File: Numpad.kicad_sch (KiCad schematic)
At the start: 107 parts, among them J1 USB_C_Receptacle_USB2.0, J3 AVR-ISP-6, Q2 DMN2041L, SW10 SW_Push, SW11 SW_Push, SW12 SW_Push, SW13 SW_Push, SW14 SW_Push, SW15 SW_Push, SW16 SW_Push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

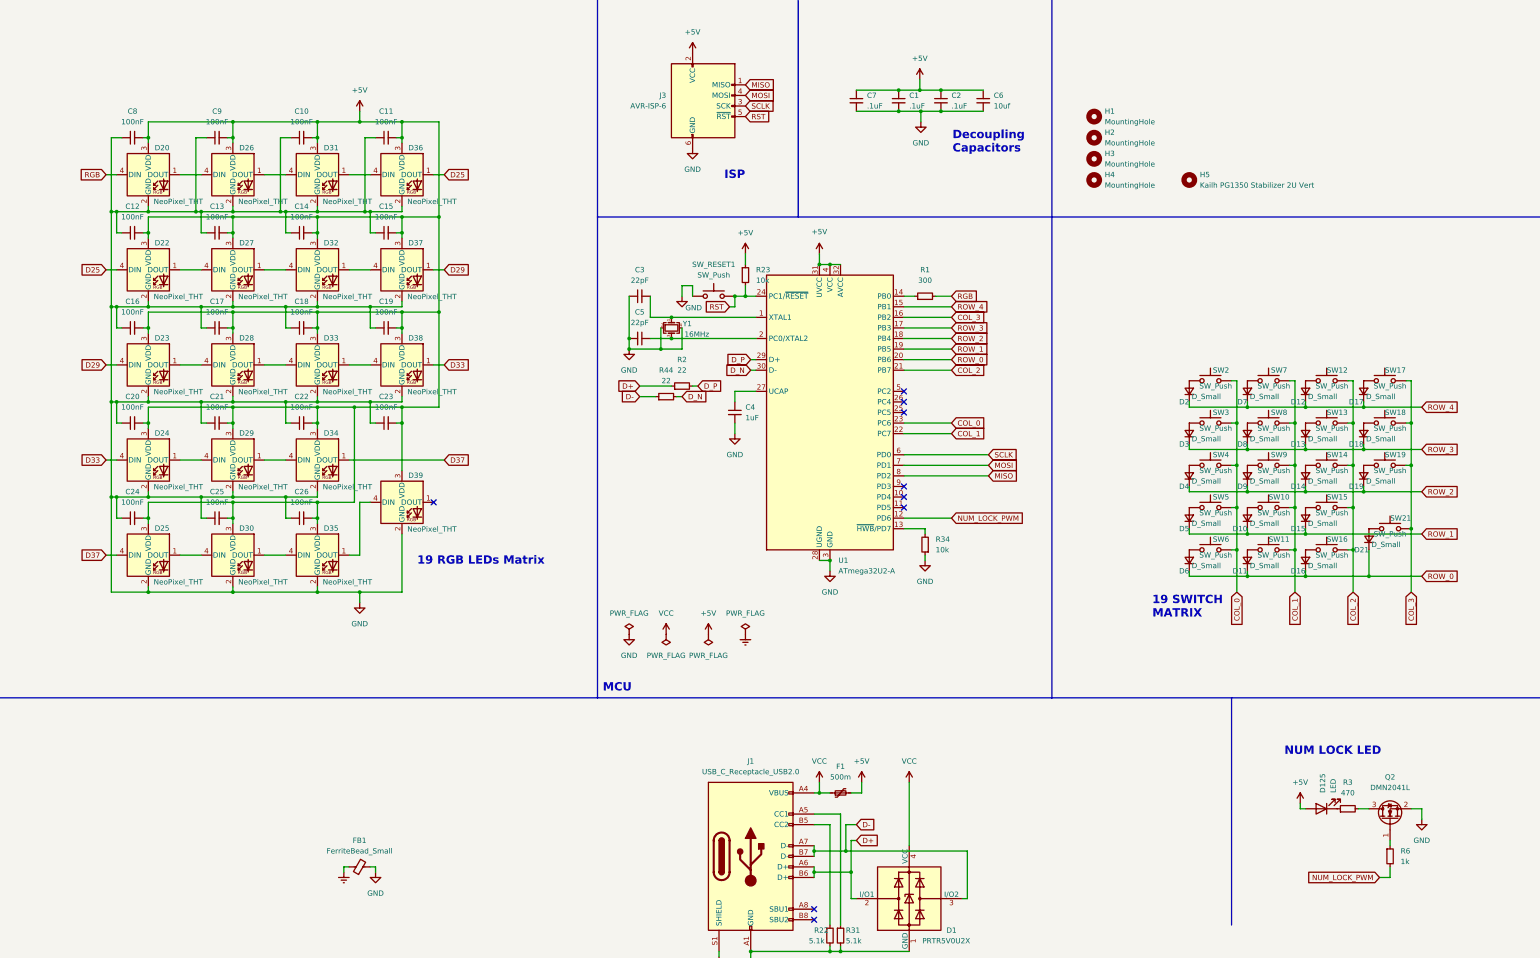
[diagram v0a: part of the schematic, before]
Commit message: replaced LEDs with RGBs, and started the PCB for keyboard
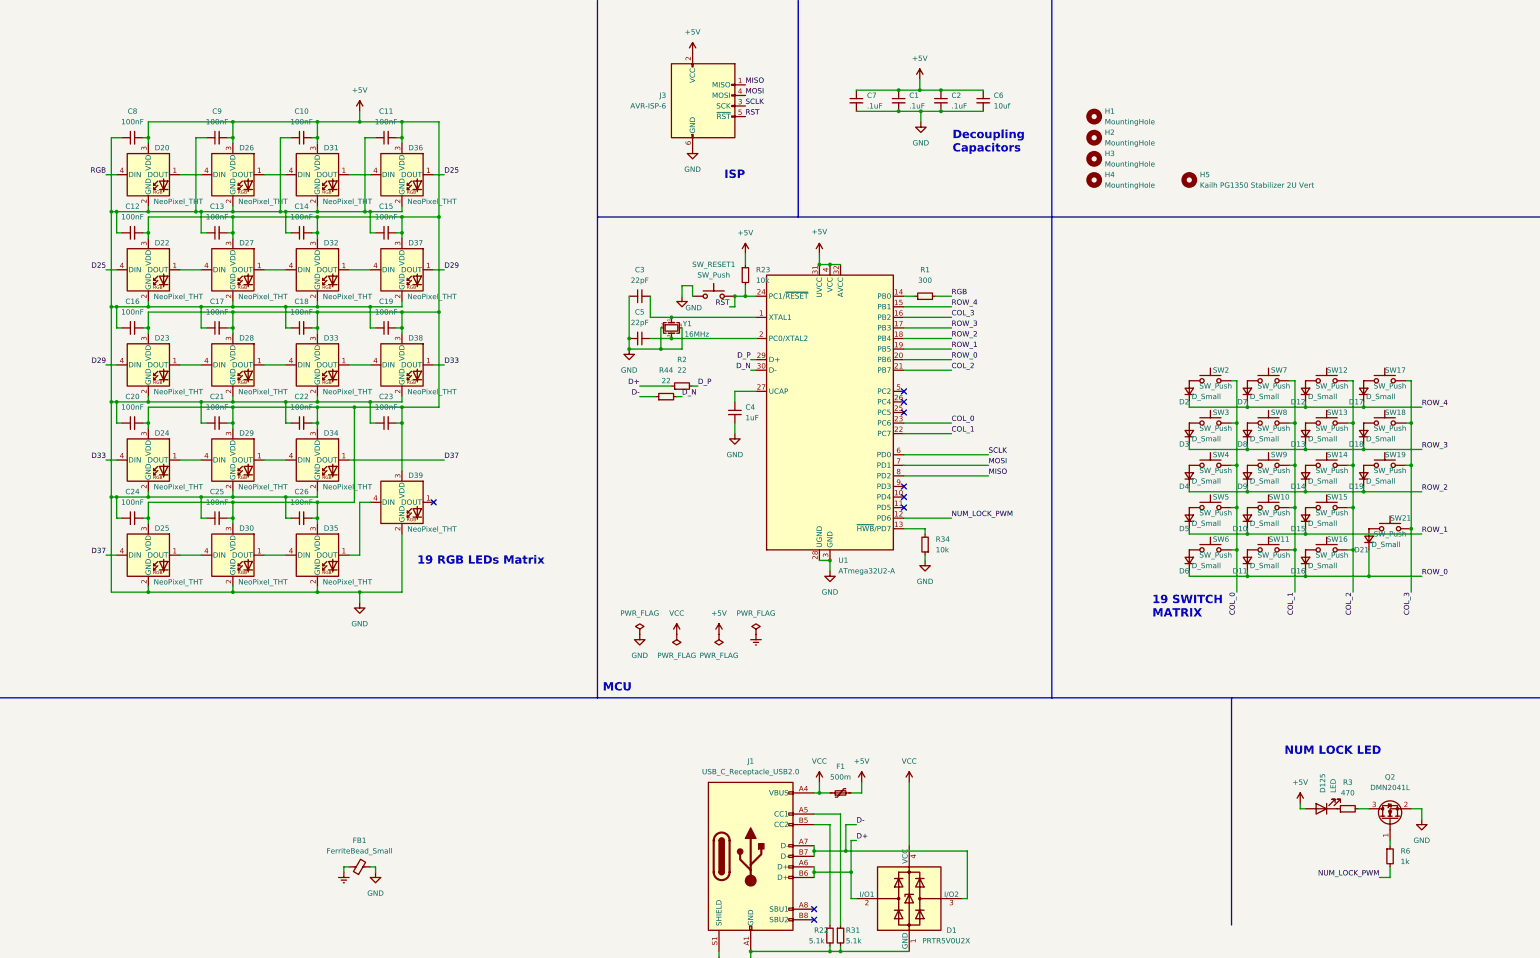
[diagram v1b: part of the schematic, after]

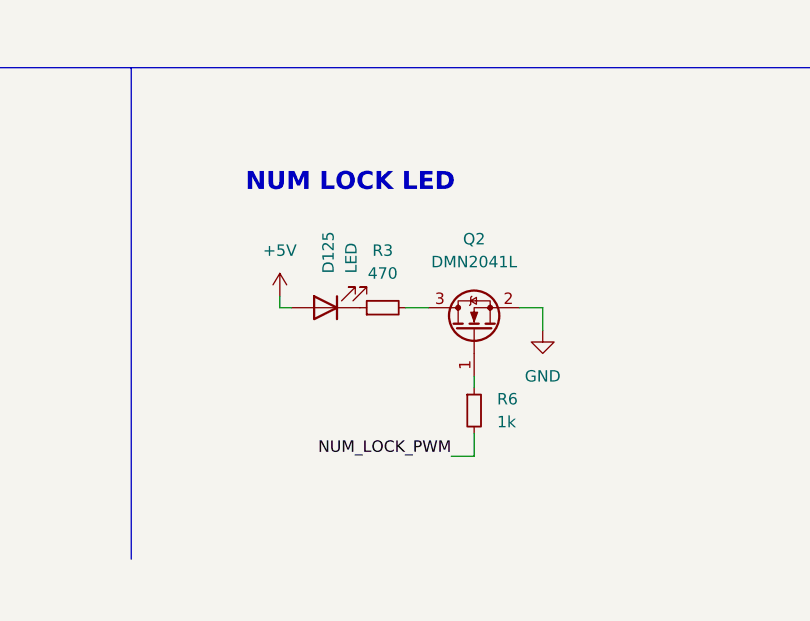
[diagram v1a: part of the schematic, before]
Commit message: did some via adjustments and decided to not go ahead with num lock light
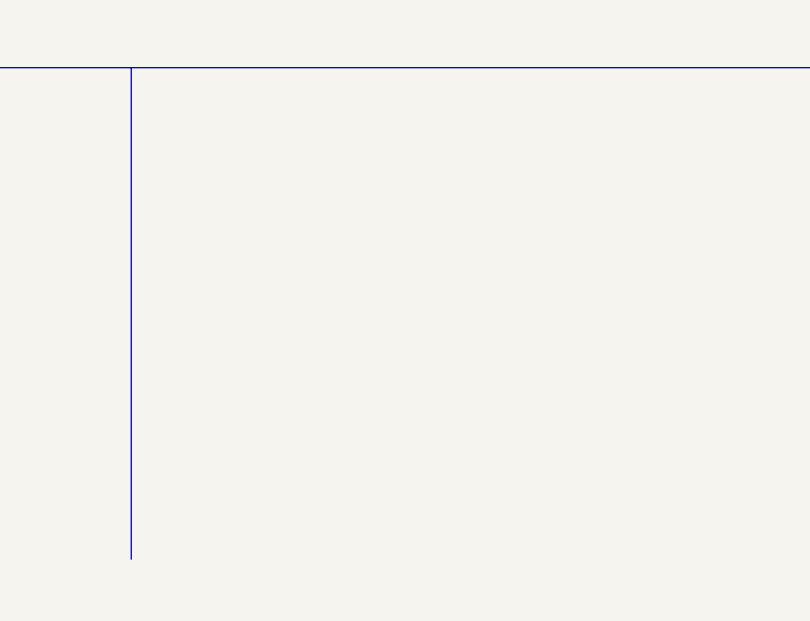
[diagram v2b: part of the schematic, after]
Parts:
- removed D125: LED, LED_SMD:LED_PLCC_2835, symbol Device:LED
- removed Q2: DMN2041L, Package_TO_SOT_SMD:SOT-23, symbol Transistor_FET:DMN2041L
- removed R3: 470, Resistor_SMD:R_0402_1005Metric, symbol Device:R_Small
- removed R6: 1k, Resistor_SMD:R_0402_1005Metric, symbol Device:R_Small
- SW21: footprint keyswitches.pretty-2:Kailh_socket_PG1350 -> keyswitches.pretty-2:Kailh_socket_PG1350_2U_Vert
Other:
- note removed: "NUM LOCK LED"
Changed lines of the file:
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@@
     (stroke (width 0) (type default) (color 0 0 0 0))
   )
-  (wire (pts (xy 342.9 207.01) (xy 345.44 207.01))
-    (stroke (width 0) (type default) (color 0 0 0 0))
-  )
   (wire (pts (xy 92.71 110.49) (xy 101.6 110.49))
     (stroke (width 0) (type default) (color 0 0 0 0))
@@
     (stroke (width 0) (type default) (color 0 0 0 0))
   )
-  (wire (pts (xy 350.52 215.9) (xy 350.52 214.63))
-    (stroke (width 0) (type default) (color 0 0 0 0))
-  )
   (wire (pts (xy 340.36 114.3) (xy 341.63 114.3))
     (stroke (width 0) (type default) (color 0 0 0 0))
@@
     (stroke (width 0) (type default) (color 0 0 0 0))
   )
-  (wire (pts (xy 350.52 223.52) (xy 350.52 220.98))
-    (stroke (width 0) (type default) (color 0 0 0 0))
-  )
   (wire (pts (xy 212.09 222.25) (xy 212.09 223.52))
     (stroke (width 0) (type default) (color 0 0 0 0))
   )
-  (wire (pts (xy 328.93 207.01) (xy 330.2 207.01))
-    (stroke (width 0) (type default) (color 0 0 0 0))
-  )
   (wire (pts (xy 302.26 110.49) (xy 316.23 110.49))
     (stroke (width 0) (type default) (color 0 0 0 0))
@@
     (stroke (width 0) (type default) (color 0 0 0 0))
   )
-  (wire (pts (xy 358.14 207.01) (xy 358.14 209.55))
-    (stroke (width 0) (type default) (color 0 0 0 0))
-  )
   (wire (pts (xy 52.07 86.36) (xy 64.77 86.36))
     (stroke (width 0) (type default) (color 0 0 0 0))
@@
     (stroke (width 0) (type default) (color 0 0 0 0))
   )
-  (wire (pts (xy 355.6 207.01) (xy 358.14 207.01))
-    (stroke (width 0) (type default) (color 0 0 0 0))
-  )
   (wire (pts (xy 92.71 133.35) (xy 101.6 133.35))
     (stroke (width 0) (type default) (color 0 0 0 0))
@@
     (stroke (width 0) (type default) (color 0 0 0 0))
   )
-  (wire (pts (xy 328.93 205.74) (xy 328.93 207.01))
-    (stroke (width 0) (type default) (color 0 0 0 0))
-  )
   (wire (pts (xy 92.71 133.35) (xy 92.71 137.16))
     (stroke (width 0) (type default) (color 0 0 0 0))
@@
     (stroke (width 0) (type default) (color 0 0 0 0))
   )
-  (wire (pts (xy 350.52 223.52) (xy 347.98 223.52))
-    (stroke (width 0) (type default) (color 0 0 0 0))
-  )
   (wire (pts (xy 91.44 45.72) (xy 92.71 45.72))
     (stroke (width 0) (type default) (color 0 0 0 0))
@@
     (effects (font (size 2 2) (thickness 0.4) bold) (justify left bottom))
   )
-  (text "NUM LOCK LED" (at 325.12 194.31 0)
-    (effects (font (size 2 2) (thickness 0.4) bold) (justify left bottom))
-  )
   (text "MCU" (at 161.29 179.07 0)
     (effects (font (size 2 2) (thickness 0.4) bold) (justify left bottom))
@@
     (effects (font (size 1.27 1.27)) (justify left bottom))
   )
-  (label "NUM_LOCK_PWM" (at 347.98 223.52 180)
-    (effects (font (size 1.27 1.27)) (justify right bottom))
-  )
   (label "COL_0" (at 313.69 154.94 270)
     (effects (font (size 1.27 1.27)) (justify right bottom))
@@
     (pin "2")
   )
-  (symbol (lib_id "power:+5V") (at 328.93 205.74 0) (unit 1)
-    (in_bom yes) (on_board yes) (fields_autoplaced)
-    (property "Reference" "#PWR01" (id 0) (at 328.93 209.55 0)
-      (effects (font (size 1.27 1.27)) hide)
-    )
-    (property "Value" "+5V" (id 1) (at 328.93 200.66 0))
-    (property "Footprint" "" (id 2) (at 328.93 205.74 0)
-      (effects (font (size 1.27 1.27)) hide)
-    )
-    (property "Datasheet" "" (id 3) (at 328.93 205.74 0)
-      (effects (font (size 1.27 1.27)) hide)
-    )
-    (pin "1")
-  )
   (symbol (lib_id "Device:D_Small") (at 344.17 116.84 90) (unit 1)
     (in_bom yes) (on_board yes) (fields_autoplaced)
@@
     (pin "4")
   )
-  (symbol (lib_id "Device:R_Small") (at 350.52 218.44 0) (unit 1)
-    (in_bom yes) (on_board yes) (fields_autoplaced)
-    (property "Reference" "R6" (id 0) (at 353.06 217.1699 0)
-      (effects (font (size 1.27 1.27)) (justify left))
-    )
-    (property "Value" "1k" (id 1) (at 353.06 219.7099 0)
-      (effects (font (size 1.27 1.27)) (justify left))
-    )
-    (property "Footprint" "Resistor_SMD:R_0402_1005Metric" (id 2) (at 350.52 218.44 0)
-      (effects (font (size 1.27 1.27)) hide)
-    )
-    (property "Datasheet" "~" (id 3) (at 350.52 218.44 0)
-      (effects (font (size 1.27 1.27)) hide)
-    )
-    (pin "1")
-    (pin "2")
-  )
   (symbol (lib_id "power:PWR_FLAG") (at 189.23 165.1 180) (unit 1)
     (in_bom yes) (on_board yes) (fields_autoplaced)
@@
     (pin "2")
   )
-  (symbol (lib_id "Device:R_Small") (at 340.36 207.01 90) (unit 1)
-    (in_bom yes) (on_board yes) (fields_autoplaced)
-    (property "Reference" "R3" (id 0) (at 340.36 200.66 90))
-    (property "Value" "470" (id 1) (at 340.36 203.2 90))
-    (property "Footprint" "Resistor_SMD:R_0402_1005Metric" (id 2) (at 340.36 207.01 0)
-      (effects (font (size 1.27 1.27)) hide)
-    )
-    (property "Datasheet" "~" (id 3) (at 340.36 207.01 0)
-      (effects (font (size 1.27 1.27)) hide)
-    )
-    (pin "1")
-    (pin "2")
-  )
   (symbol (lib_id "Switch:SW_Push") (at 307.34 104.14 0) (unit 1)
     (in_bom yes) (on_board yes) (fields_autoplaced)
@@
     (pin "1")
   )
-  (symbol (lib_id "power:GND") (at 358.14 209.55 0) (unit 1)
-    (in_bom yes) (on_board yes) (fields_autoplaced)
-    (property "Reference" "#PWR02" (id 0) (at 358.14 215.9 0)
-      (effects (font (size 1.27 1.27)) hide)
-    )
-    (property "Value" "GND" (id 1) (at 358.14 214.63 0))
-    (property "Footprint" "" (id 2) (at 358.14 209.55 0)
-      (effects (font (size 1.27 1.27)) hide)
-    )
-    (property "Datasheet" "" (id 3) (at 358.14 209.55 0)
-      (effects (font (size 1.27 1.27)) hide)
-    )
-    (pin "1")
-  )
   (symbol (lib_id "Device:R_Small") (at 215.9 237.49 0) (unit 1)
     (in_bom yes) (on_board yes)
@@
     (pin "1")
   )
-  (symbol (lib_id "Device:LED") (at 334.01 207.01 180) (unit 1)
-    (in_bom yes) (on_board yes)
-    (property "Reference" "D125" (id 0) (at 334.3274 203.2 90)
-      (effects (font (size 1.27 1.27)) (justify right))
-    )
-    (property "Value" "LED" (id 1) (at 336.8674 203.2 90)
-      (effects (font (size 1.27 1.27)) (justify right))
-    )
-    (property "Footprint" "LED_SMD:LED_PLCC_2835" (id 2) (at 334.01 207.01 0)
-      (effects (font (size 1.27 1.27)) hide)
-    )
-    (property "Datasheet" "~" (id 3) (at 334.01 207.01 0)
-      (effects (font (size 1.27 1.27)) hide)
-    )
-    (pin "1")
-    (pin "2")
-  )
   (symbol (lib_id "Device:C_Small") (at 48.26 68.58 90) (unit 1)
     (in_bom yes) (on_board yes) (fields_autoplaced)
@@
     (pin "2")
   )
-  (symbol (lib_id "Transistor_FET:DMN2041L") (at 350.52 209.55 90) (unit 1)
-    (in_bom yes) (on_board yes) (fields_autoplaced)
-    (property "Reference" "Q2" (id 0) (at 350.52 199.39 90))
-    (property "Value" "DMN2041L" (id 1) (at 350.52 201.93 90))
-    (property "Footprint" "Package_TO_SOT_SMD:SOT-23" (id 2) (at 352.425 204.47 0)
-      (effects (font (size 1.27 1.27) italic) (justify left) hide)
-    )
-    (property "Datasheet" "https://www.diodes.com/assets/Datasheets/products_inactive_data/DMN2041L.pdf" (id 3) (at 350.52 209.55 0)
-      (effects (font (size 1.27 1.27)) (justify left) hide)
-    )
-    (pin "1")
-    (pin "2")
-    (pin "3")
-  )
   (symbol (lib_id "LED:NeoPixel_THT") (at 92.71 123.19 0) (unit 1)
     (in_bom yes) (on_board yes)
@@
     (property "Reference" "SW21" (id 0) (at 353.06 137.16 0))
     (property "Value" "SW_Push" (id 1) (at 350.52 140.97 0))
-    (property "Footprint" "keyswitches.pretty-2:Kailh_socket_PG1350" (id 2) (at 350.52 134.62 0)
+    (property "Footprint" "keyswitches.pretty-2:Kailh_socket_PG1350_2U_Vert" (id 2) (at 350.52 134.62 0)
       (effects (font (size 1.27 1.27)) hide)
     )
@@
       (reference "#FLG0104") (unit 1) (value "PWR_FLAG") (footprint "")
     )
-    (path "/0a78ad03-beb3-4d07-99c9-0a27e06bfc43"
-      (reference "#PWR01") (unit 1) (value "+5V") (footprint "")
-    )
-    (path "/72ee0188-de07-46ee-8ace-5fccc2a451eb"
-      (reference "#PWR02") (unit 1) (value "GND") (footprint "")
-    )
     (path "/b908e591-f332-45a7-856b-24459849375a"
       (reference "#PWR03") (unit 1) (value "GND") (footprint "")
@@
       (reference "D39") (unit 1) (value "NeoPixel_THT") (footprint "kicad-keyboard-parts.pretty:LED_RGB_Wuerth-PLCC4_3.2x2.8mm_150141M173100")
     )
-    (path "/79691aaa-5d20-4e18-946b-f54c0a64d8b9"
-      (reference "D125") (unit 1) (value "LED") (footprint "LED_SMD:LED_PLCC_2835")
-    )
     (path "/ba184852-e764-4a49-b8bb-08eae1e2e546"
       (reference "F1") (unit 1) (value "500m") (footprint "Keebio-Parts:Fuse_0805")
@@
       (reference "J3") (unit 1) (value "AVR-ISP-6") (footprint "Keebio-Parts:ICSP-Header")
     )
-    (path "/a10efd7b-de7b-4f55-8e6b-70f75dfb7643"
-      (reference "Q2") (unit 1) (value "DMN2041L") (footprint "Package_TO_SOT_SMD:SOT-23")
-    )
     (path "/67d3a646-e90d-44d6-8f93-5abfb37ecc0b"
       (reference "R1") (unit 1) (value "300") (footprint "Resistor_SMD:R_0402_1005Metric")
@@
       (reference "R2") (unit 1) (value "22") (footprint "Resistor_SMD:R_0402_1005Metric")
     )
-    (path "/4c88ea76-895f-44b9-a038-40a4f110c62e"
-      (reference "R3") (unit 1) (value "470") (footprint "Resistor_SMD:R_0402_1005Metric")
-    )
-    (path "/2c217653-ec43-43b0-bc28-c0c2b4ca3f6e"
-      (reference "R6") (unit 1) (value "1k") (footprint "Resistor_SMD:R_0402_1005Metric")
-    )
     (path "/7440c7ff-e379-4480-869d-0b9d87746774"
       (reference "R22") (unit 1) (value "5.1k") (footprint "Resistor_SMD:R_0402_1005Metric")
@@
     )
     (path "/cccd222e-cea2-42b0-b1d9-9cf7766b7c07"
-      (reference "SW21") (unit 1) (value "SW_Push") (footprint "keyswitches.pretty-2:Kailh_socket_PG1350")
+      (reference "SW21") (unit 1) (value "SW_Push") (footprint "keyswitches.pretty-2:Kailh_socket_PG1350_2U_Vert")
     )
     (path "/9175ce73-cae1-4cca-a0dd-98fd6e4776f9"
